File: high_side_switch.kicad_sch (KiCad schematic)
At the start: 5 parts, among them Q1 NCE60P25K, Q2 2N7002-7-F

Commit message: resolved align to grid warnings
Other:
- moved on the sheet: Q1, Q2, R24, R26, R27

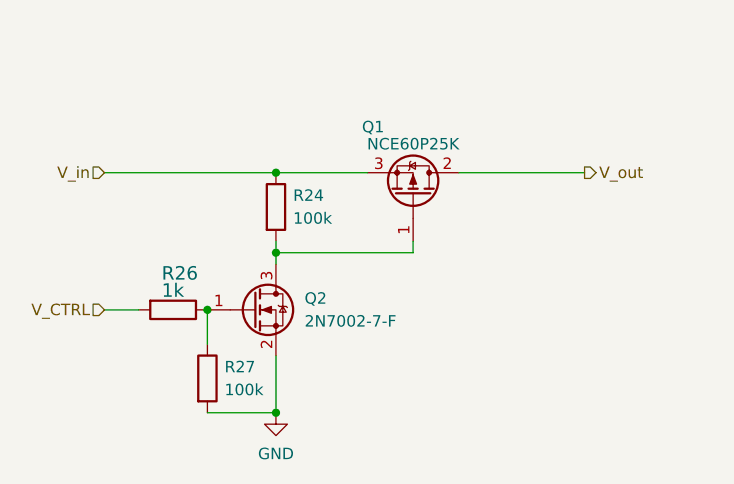
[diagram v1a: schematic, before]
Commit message: 0.25 mm clearance for silk; GND plane clearance to 0.25 mm; added gate protection for high side switch
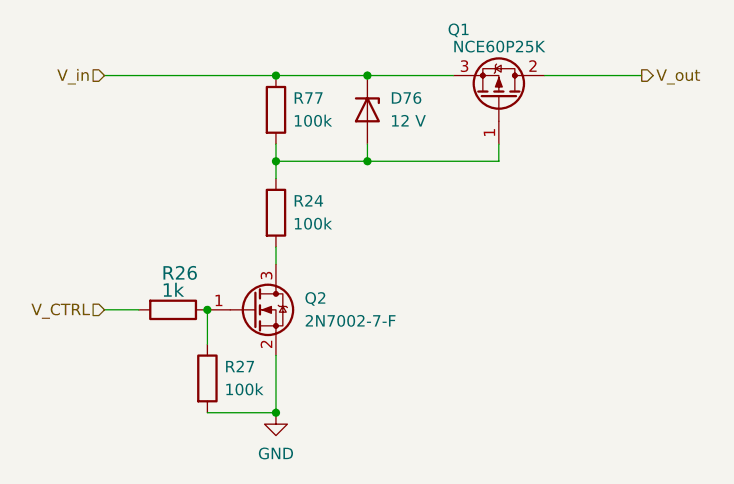
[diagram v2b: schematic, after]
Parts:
- added D76: 12 V, Diode_SMD:D_SOD-123, symbol Device:D_Zener
- added R77: 100k, Resistor_SMD:R_0603_1608Metric, symbol Device:R
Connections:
- net V_in: now also D76.1 (K), R77.1; no longer R24.1
- net at Q2.3 (D), R24.2: no longer Q1.1 (G)
- new net: D76.2 (A), Q1.1 (G), R24.1, R77.2
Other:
- moved on the sheet: Q1, R24
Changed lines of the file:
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@@
 (kicad_sch (version 20230121) (generator eeschema)
   (paper "A4")
+  (junction (at 148.59 82.55) (diameter 0) (color 0 0 0 0)
+  )
   (junction (at 138.43 110.49) (diameter 0) (color 0 0 0 0)
   )
-  (junction (at 138.43 83.82) (diameter 0) (color 0 0 0 0)
-  )
-  (junction (at 138.43 92.71) (diameter 0) (color 0 0 0 0)
+  (junction (at 148.59 73.025) (diameter 0) (color 0 0 0 0)
+  )
+  (junction (at 138.43 82.55) (diameter 0) (color 0 0 0 0)
   )
   (junction (at 130.81 99.06) (diameter 0) (color 0 0 0 0)
   )
+  (junction (at 138.43 73.025) (diameter 0) (color 0 0 0 0)
+  )
   (wire (pts (xy 138.43 104.14) (xy 138.43 110.49))
     (stroke (width 0) (type default))
   )
-  (wire (pts (xy 138.43 92.71) (xy 138.43 93.98))
-    (stroke (width 0) (type default))
-  )
-  (wire (pts (xy 158.75 83.82) (xy 172.72 83.82))
-    (stroke (width 0) (type default))
-  )
-  (wire (pts (xy 153.67 92.71) (xy 153.67 91.44))
-    (stroke (width 0) (type default))
-  )
-  (wire (pts (xy 119.38 83.82) (xy 138.43 83.82))
+  (wire (pts (xy 138.43 92.075) (xy 138.43 93.98))
+    (stroke (width 0) (type default))
+  )
+  (wire (pts (xy 163.195 80.645) (xy 163.195 82.55))
+    (stroke (width 0) (type default))
+  )
+  (wire (pts (xy 148.59 80.645) (xy 148.59 82.55))
+    (stroke (width 0) (type default))
+  )
+  (wire (pts (xy 138.43 82.55) (xy 138.43 84.455))
+    (stroke (width 0) (type default))
+  )
+  (wire (pts (xy 168.275 73.025) (xy 179.07 73.025))
+    (stroke (width 0) (type default))
+  )
+  (wire (pts (xy 148.59 82.55) (xy 138.43 82.55))
+    (stroke (width 0) (type default))
+  )
+  (wire (pts (xy 138.43 80.645) (xy 138.43 82.55))
+    (stroke (width 0) (type default))
+  )
+  (wire (pts (xy 158.115 73.025) (xy 148.59 73.025))
+    (stroke (width 0) (type default))
+  )
+  (wire (pts (xy 119.38 73.025) (xy 138.43 73.025))
     (stroke (width 0) (type default))
   )
@@
     (stroke (width 0) (type default))
   )
-  (wire (pts (xy 138.43 91.44) (xy 138.43 92.71))
-    (stroke (width 0) (type default))
-  )
-  (wire (pts (xy 138.43 83.82) (xy 148.59 83.82))
-    (stroke (width 0) (type default))
-  )
-  (wire (pts (xy 138.43 92.71) (xy 153.67 92.71))
+  (wire (pts (xy 163.195 82.55) (xy 148.59 82.55))
+    (stroke (width 0) (type default))
+  )
+  (wire (pts (xy 138.43 73.025) (xy 148.59 73.025))
     (stroke (width 0) (type default))
   )
@@
     (stroke (width 0) (type default))
   )
-  (hierarchical_label "V_in" (shape input) (at 119.38 83.82 180) (fields_autoplaced)
+  (hierarchical_label "V_in" (shape input) (at 119.38 73.025 180) (fields_autoplaced)
     (effects (font (size 1.27 1.27)) (justify right))
   )
-  (hierarchical_label "V_out" (shape output) (at 172.72 83.82 0) (fields_autoplaced)
+  (hierarchical_label "V_out" (shape output) (at 179.07 73.025 0) (fields_autoplaced)
     (effects (font (size 1.27 1.27)) (justify left))
   )
@@
     (effects (font (size 1.27 1.27)) (justify right))
   )
-  (symbol (lib_id "Device:R") (at 138.43 87.63 0) (unit 1)
-    (in_bom yes) (on_board yes) (dnp no) (fields_autoplaced)
-    (property "Reference" "R24" (at 140.335 86.3599 0)
-      (effects (font (size 1.27 1.27)) (justify left))
-    )
-    (property "Value" "100k" (at 140.335 88.8999 0)
-      (effects (font (size 1.27 1.27)) (justify left))
-    )
-    (property "Footprint" "Resistor_SMD:R_0603_1608Metric" (at 136.652 87.63 90)
-      (effects (font (size 1.27 1.27)) hide)
-    )
-    (property "Datasheet" "https://datasheet.lcsc.com/lcsc/2206010045_UNI-ROYAL-Uniroyal-Elec-0603WAF1003T5E_C25803.pdf" (at 138.43 87.63 0)
-      (effects (font (size 1.27 1.27)) hide)
-    )
-    (property "LCSC Part" "C25803" (at 138.43 87.63 90)
+  (symbol (lib_id "Device:R") (at 138.43 88.265 0) (unit 1)
+    (in_bom yes) (on_board yes) (dnp no) (fields_autoplaced)
+    (property "Reference" "R24" (at 140.335 86.9949 0)
+      (effects (font (size 1.27 1.27)) (justify left))
+    )
+    (property "Value" "100k" (at 140.335 89.5349 0)
+      (effects (font (size 1.27 1.27)) (justify left))
+    )
+    (property "Footprint" "Resistor_SMD:R_0603_1608Metric" (at 136.652 88.265 90)
+      (effects (font (size 1.27 1.27)) hide)
+    )
+    (property "Datasheet" "https://datasheet.lcsc.com/lcsc/2206010045_UNI-ROYAL-Uniroyal-Elec-0603WAF1003T5E_C25803.pdf" (at 138.43 88.265 0)
+      (effects (font (size 1.27 1.27)) hide)
+    )
+    (property "LCSC Part" "C25803" (at 138.43 88.265 90)
       (effects (font (size 1.27 1.27)) hide)
     )
@@
         (path "/ebe87c89-9c25-4dbf-a80d-e2428f6eb240/4bfc1dae-8815-428b-9f5b-0a18ce8bea6c/35179495-37d7-47de-ba96-29dd2062304a"
           (reference "R64") (unit 1)
+        )
+      )
+    )
+  )
+  (symbol (lib_id "Device:D_Zener") (at 148.59 76.835 270) (unit 1)
+    (in_bom yes) (on_board yes) (dnp no) (fields_autoplaced)
+    (property "Reference" "D76" (at 151.13 75.565 90)
+      (effects (font (size 1.27 1.27)) (justify left))
+    )
+    (property "Value" "12 V" (at 151.13 78.105 90)
+      (effects (font (size 1.27 1.27)) (justify left))
+    )
+    (property "Footprint" "Diode_SMD:D_SOD-123" (at 148.59 76.835 0)
+      (effects (font (size 1.27 1.27)) hide)
+    )
+    (property "Datasheet" "https://datasheet.lcsc.com/lcsc/2304140030_Diodes-Incorporated-DDZ12C-7_C151340.pdf" (at 148.59 76.835 0)
+      (effects (font (size 1.27 1.27)) hide)
+    )
+    (property "LCSC Part" "C151340" (at 148.59 76.835 90)
+      (effects (font (size 1.27 1.27)) hide)
+    )
+    (pin "1")
+    (pin "2")
+    (instances
+      (project "mainboard"
+        (path "/ebe87c89-9c25-4dbf-a80d-e2428f6eb240/4bfc1dae-8815-428b-9f5b-0a18ce8bea6c/90d932d0-2c7e-4845-b9b6-e3fdf2e1c4ae"
+          (reference "D76") (unit 1)
+        )
+        (path "/ebe87c89-9c25-4dbf-a80d-e2428f6eb240/4bfc1dae-8815-428b-9f5b-0a18ce8bea6c/262fe21c-2d6f-494e-b4ac-8e9e705153fd"
+          (reference "D74") (unit 1)
+        )
+        (path "/ebe87c89-9c25-4dbf-a80d-e2428f6eb240/4bfc1dae-8815-428b-9f5b-0a18ce8bea6c/7fd296be-2a42-4c0e-8077-865195ad1c40"
+          (reference "D75") (unit 1)
+        )
+        (path "/ebe87c89-9c25-4dbf-a80d-e2428f6eb240/4bfc1dae-8815-428b-9f5b-0a18ce8bea6c/35179495-37d7-47de-ba96-29dd2062304a"
+          (reference "D77") (unit 1)
         )
       )
@@
     )
   )
-  (symbol (lib_id "Device:Q_PMOS_GDS") (at 153.67 86.36 270) (mirror x) (unit 1)
+  (symbol (lib_id "Device:Q_PMOS_GDS") (at 163.195 75.565 270) (mirror x) (unit 1)
     (in_bom yes) (on_board yes) (dnp no)
-    (property "Reference" "Q1" (at 149.225 78.74 90)
+    (property "Reference" "Q1" (at 158.75 67.945 90)
       (effects (font (size 1.27 1.27)))
     )
-    (property "Value" "NCE60P25K" (at 153.67 80.645 90)
+    (property "Value" "NCE60P25K" (at 163.195 69.85 90)
       (effects (font (size 1.27 1.27)))
     )
-    (property "Footprint" "Package_TO_SOT_SMD:TO-252-2" (at 156.21 81.28 0)
-      (effects (font (size 1.27 1.27)) hide)
-    )
-    (property "Datasheet" "https://datasheet.lcsc.com/lcsc/1810241809_Wuxi-NCE-Power-Semiconductor-NCE60P25K_C130105.pdf" (at 153.67 86.36 0)
-      (effects (font (size 1.27 1.27)) hide)
-    )
-    (property "LCSC Part" "C130105" (at 153.67 86.36 90)
+    (property "Footprint" "Package_TO_SOT_SMD:TO-252-2" (at 165.735 70.485 0)
+      (effects (font (size 1.27 1.27)) hide)
+    )
+    (property "Datasheet" "https://datasheet.lcsc.com/lcsc/1810241809_Wuxi-NCE-Power-Semiconductor-NCE60P25K_C130105.pdf" (at 163.195 75.565 0)
+      (effects (font (size 1.27 1.27)) hide)
+    )
+    (property "LCSC Part" "C130105" (at 163.195 75.565 90)
       (effects (font (size 1.27 1.27)) hide)
     )
@@
         )
       )
+    )
+  )
+  (symbol (lib_id "Device:R") (at 138.43 76.835 0) (unit 1)
+    (in_bom yes) (on_board yes) (dnp no) (fields_autoplaced)
+    (property "Reference" "R77" (at 140.335 75.5649 0)
+      (effects (font (size 1.27 1.27)) (justify left))
+    )
+    (property "Value" "100k" (at 140.335 78.1049 0)
+      (effects (font (size 1.27 1.27)) (justify left))
+    )
+    (property "Footprint" "Resistor_SMD:R_0603_1608Metric" (at 136.652 76.835 90)
+      (effects (font (size 1.27 1.27)) hide)
+    )
+    (property "Datasheet" "https://datasheet.lcsc.com/lcsc/2206010045_UNI-ROYAL-Uniroyal-Elec-0603WAF1003T5E_C25803.pdf" (at 138.43 76.835 0)
+      (effects (font (size 1.27 1.27)) hide)
+    )
+    (property "LCSC Part" "C25803" (at 138.43 76.835 90)
+      (effects (font (size 1.27 1.27)) hide)
+    )
+    (pin "1")
+    (pin "2")
+    (instances
+      (project "mainboard"
+        (path "/ebe87c89-9c25-4dbf-a80d-e2428f6eb240/4bfc1dae-8815-428b-9f5b-0a18ce8bea6c/262fe21c-2d6f-494e-b4ac-8e9e705153fd"
+          (reference "R77") (unit 1)
+        )
+        (path "/ebe87c89-9c25-4dbf-a80d-e2428f6eb240/4bfc1dae-8815-428b-9f5b-0a18ce8bea6c/7fd296be-2a42-4c0e-8077-865195ad1c40"
+          (reference "R78") (unit 1)
+        )
+        (path "/ebe87c89-9c25-4dbf-a80d-e2428f6eb240/4bfc1dae-8815-428b-9f5b-0a18ce8bea6c/90d932d0-2c7e-4845-b9b6-e3fdf2e1c4ae"
+          (reference "R79") (unit 1)
+        )
+        (path "/ebe87c89-9c25-4dbf-a80d-e2428f6eb240/4bfc1dae-8815-428b-9f5b-0a18ce8bea6c/35179495-37d7-47de-ba96-29dd2062304a"
+          (reference "R80") (unit 1)
+        )
+      )

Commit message: updated drawing corner, added license
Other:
- company: (none) -> University of Tartu
- title: (none) -> High side switch
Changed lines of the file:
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@@
 (kicad_sch (version 20230121) (generator eeschema)
   (paper "A4")
+  (title_block
+    (title "High side switch")
+    (date "2023-21-11")
+    (rev "0.2.0")
+    (company "University of Tartu")
+    (comment 1 "Licensed under CERN-OHL-P")
+  )
   (junction (at 148.59 82.55) (diameter 0) (color 0 0 0 0)
   )
